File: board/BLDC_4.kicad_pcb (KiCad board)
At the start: 2 copper layers, 100 x 80 mm, 72 parts, among them IC1 ADM3052, IC2 AP65201, IC3 AP65201, P1 CONN_01X18_20, P2 SWD, P3 USB_B, P4 Power, U1 STM32F40X_LQFP64, X2 8MHz 10ppm

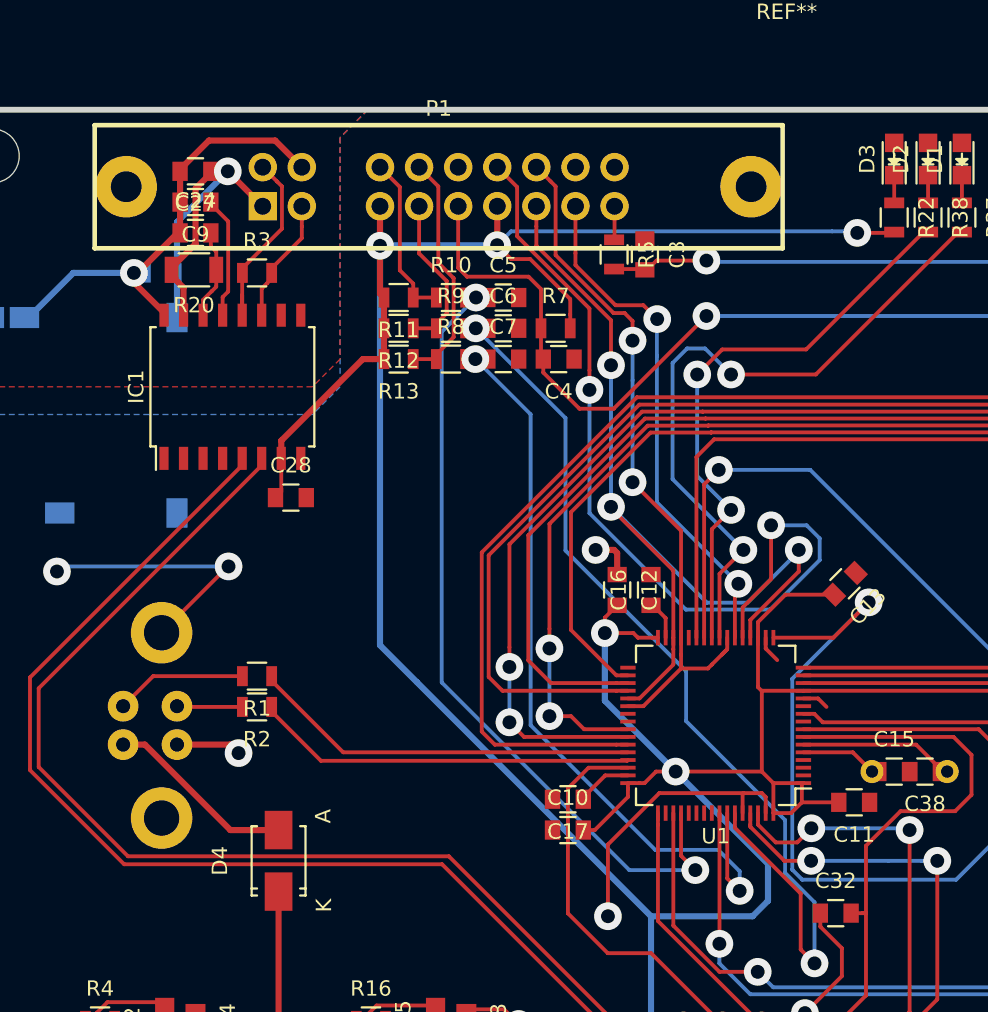
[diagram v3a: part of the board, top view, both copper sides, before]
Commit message: - small optimisations - fixed connector on wrong layer
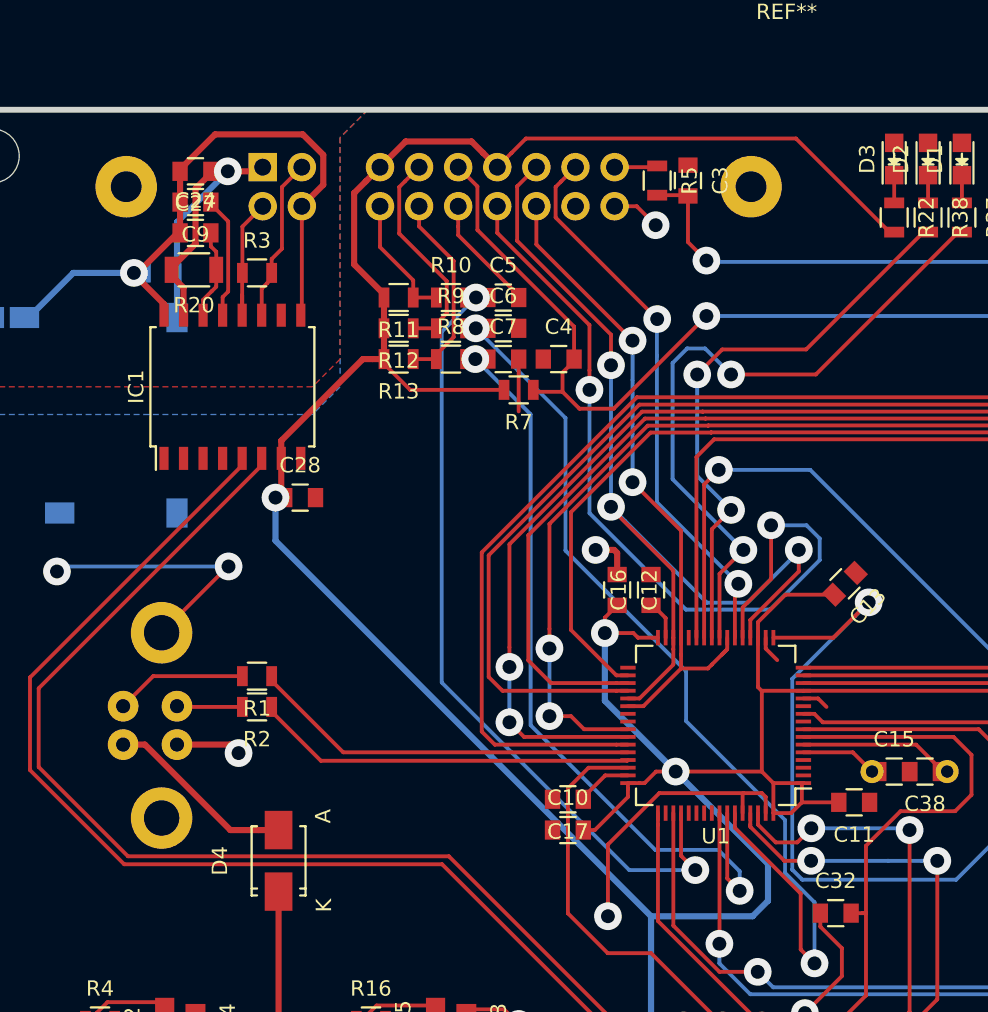
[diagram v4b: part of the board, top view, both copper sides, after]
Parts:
- P1: moved to B.Cu
- moved C3 5.56 mm to (199.0, 54.8)
- moved R5 5.56 mm to (197.0, 54.8)
- moved R7 4.66 mm to (188.0, 68.4), turned to 180 degrees
- moved C28 0.60 mm to (173.8, 75.4)
- turned C4 to 0 degrees
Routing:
- net GND: track 82.2 -> 96.2 mm, vias 13 -> 14
- net Earth: track 30.7 -> 43.1 mm
- net +3V3: track 327.3 -> 319.3 mm, vias 7 -> 5
- net /Filters/HALL2_IN: track 11.0 -> 14.6 mm
- net /MCU/TX_SDA_NSS: track 60.6 -> 64.2 mm
- net /CAN bus transceiver/CANH: track 12.5 -> 9.25 mm
- net /MCU/RX_SCL_MOSI: track 46.0 -> 43.0 mm
- net /CAN bus transceiver/CANL: track 8.16 -> 11.0 mm
- net /MCU/MISO_ADC_EXT2: track 33.6 -> 36.1 mm
- net /Filters/HALL1_IN: track 15.4 -> 12.8 mm
- net /MCU/SCK_ADC_EXT: track 56.8 -> 54.3 mm
- net /Filters/HALL3_IN: track 10.9 -> 8.32 mm
- net /Filters/TEMP_IN: track 95.4 -> 97.8 mm
- net +12VA: track 26.3 -> 25.1 mm
